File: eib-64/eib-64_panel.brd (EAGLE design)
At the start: 102 x 113 mm, 403 parts, among them J1 DF40-REC, J10 DF40-REC, J11 DF40-REC, J12 DF40-REC, J13 DF40-REC, J14 DF40-REC, J15 DF40-REC, J16 DF40-REC, J2 DF40-REC, J3 DF40-REC, J4 DF40-REC, J5 DF40-REC, J6 DF40-REC, J7 DF40-REC, J8 DF40-REC, J9 DF40-REC

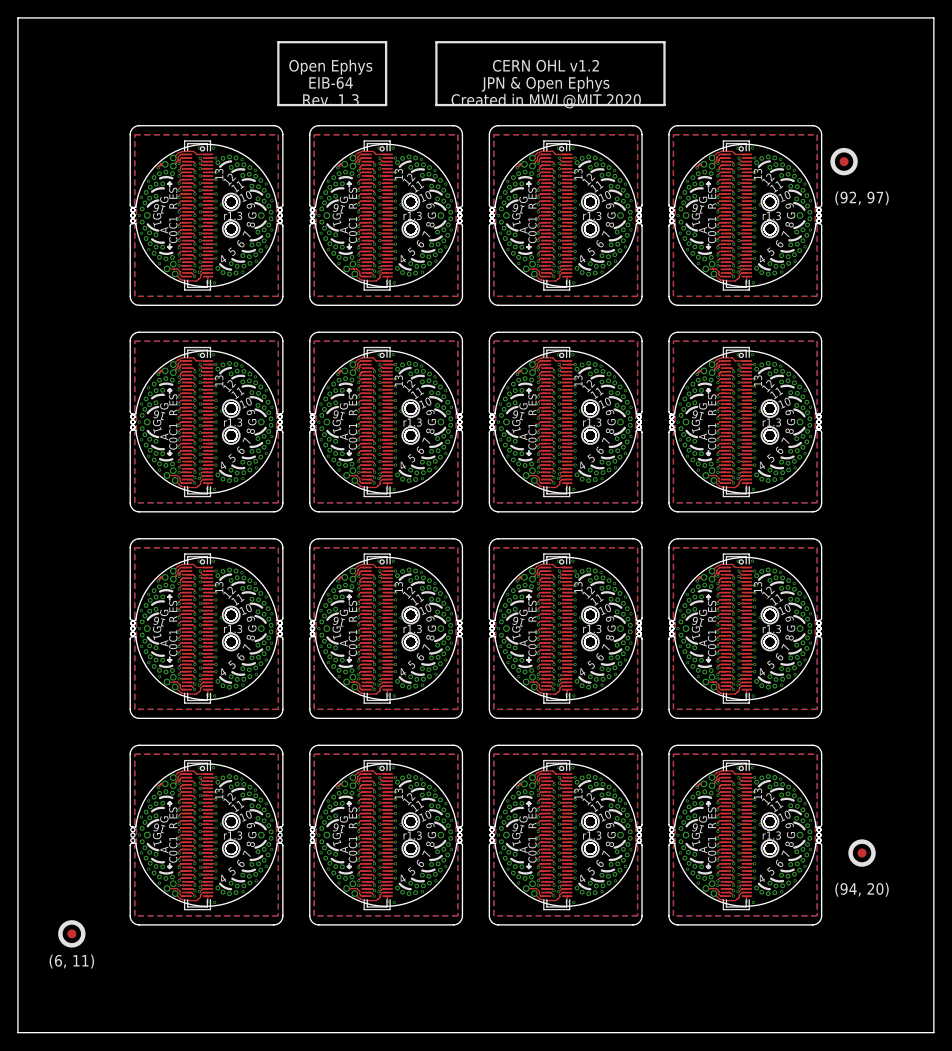
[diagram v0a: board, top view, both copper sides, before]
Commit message: Updated the panel with the new layout.
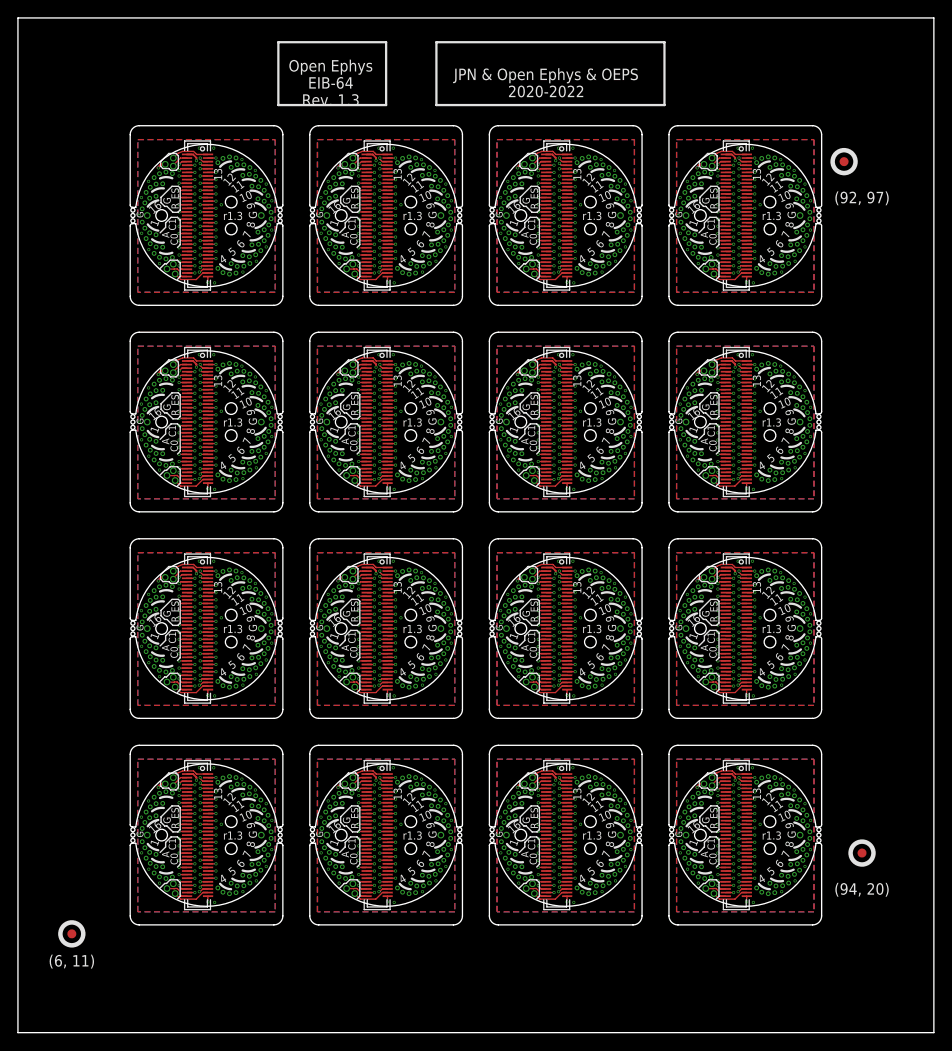
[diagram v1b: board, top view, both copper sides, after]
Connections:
- net GND: now also J1.70; no longer J1.37
- net GND1: now also J2.70; no longer J2.37
- net GND10: now also J11.70; no longer J11.37
- net GND11: now also J12.70; no longer J12.37
- net GND12: now also J13.70; no longer J13.37
- net GND13: now also J14.70; no longer J14.37
- net GND14: now also J15.70; no longer J15.37
- net GND15: now also J16.70; no longer J16.37
- net GND2: now also J3.70; no longer J3.37
- net GND3: now also J4.70; no longer J4.37
- net GND4: now also J5.70; no longer J5.37
- net GND5: now also J6.70; no longer J6.37
- net GND6: now also J7.70; no longer J7.37
- net GND7: now also J8.70; no longer J8.37
- net GND8: now also J9.70; no longer J9.37
- net GND9: now also J10.70; no longer J10.37
- net N$1: now also J1.68; no longer J1.69
- net N$10: now also J1.59; no longer J1.60
- net N$100: now also J2.37; no longer J2.38
- net N$1000: now also J16.55; no longer J16.56
- net N$1001: now also J16.54; no longer J16.55
- net N$1002: now also J16.53; no longer J16.54
- net N$1003: now also J16.52; no longer J16.53
- net N$1004: now also J16.51; no longer J16.52
- net N$1005: now also J16.50; no longer J16.51
- net N$1006: now also J16.49; no longer J16.50
- net N$1007: now also J16.48; no longer J16.49
- net N$1008: now also J16.47; no longer J16.48
- net N$1009: now also J16.46; no longer J16.47
- net N$1010: now also J16.45; no longer J16.46
- net N$1011: now also J16.44; no longer J16.45
- net N$1012: now also J16.43; no longer J16.44
- net N$1013: now also J16.42; no longer J16.43
- net N$1014: now also J16.41; no longer J16.42
- net N$1015: now also J16.40; no longer J16.41
- net N$1016: now also J16.38; no longer J16.39
- net N$1021: now also J16.65; no longer J16.66
- net N$1022: now also J16.67; no longer J16.68
- net N$1023: now also J16.39; no longer J16.40
- net N$1024: now also J16.37; no longer J16.38
- net N$11: now also J1.58; no longer J1.59
- net N$12: now also J1.57; no longer J1.58
- net N$129: now also J3.68; no longer J3.69
- net N$13: now also J1.56; no longer J1.57
- net N$130: now also J3.66; no longer J3.67
- net N$131: now also J3.64; no longer J3.65
- net N$132: now also J3.63; no longer J3.64
- net N$133: now also J3.62; no longer J3.63
- net N$134: now also J3.61; no longer J3.62
- net N$135: now also J3.60; no longer J3.61
- net N$136: now also J3.59; no longer J3.60
- net N$137: now also J3.58; no longer J3.59
- net N$138: now also J3.57; no longer J3.58
- net N$139: now also J3.56; no longer J3.57
- net N$14: now also J1.55; no longer J1.56
- net N$140: now also J3.55; no longer J3.56
- net N$141: now also J3.54; no longer J3.55
- net N$142: now also J3.53; no longer J3.54
- net N$143: now also J3.52; no longer J3.53
- net N$144: now also J3.51; no longer J3.52
- net N$145: now also J3.50; no longer J3.51
- net N$146: now also J3.49; no longer J3.50
- net N$147: now also J3.48; no longer J3.49
- net N$148: now also J3.47; no longer J3.48
- net N$149: now also J3.46; no longer J3.47
- net N$15: now also J1.54; no longer J1.55
- net N$150: now also J3.45; no longer J3.46
- net N$151: now also J3.44; no longer J3.45
- net N$152: now also J3.43; no longer J3.44
- net N$153: now also J3.42; no longer J3.43
- net N$154: now also J3.41; no longer J3.42
- net N$155: now also J3.40; no longer J3.41
- net N$156: now also J3.38; no longer J3.39
- net N$16: now also J1.53; no longer J1.54
- net N$161: now also J3.65; no longer J3.66
- net N$162: now also J3.67; no longer J3.68
- net N$163: now also J3.39; no longer J3.40
- net N$164: now also J3.37; no longer J3.38
- net N$17: now also J1.52; no longer J1.53
- net N$18: now also J1.51; no longer J1.52
- net N$19: now also J1.50; no longer J1.51
- net N$193: now also J4.68; no longer J4.69
- net N$194: now also J4.66; no longer J4.67
- net N$195: now also J4.64; no longer J4.65
- net N$196: now also J4.63; no longer J4.64
- net N$197: now also J4.62; no longer J4.63
- net N$198: now also J4.61; no longer J4.62
- net N$2: now also J1.65; no longer J1.66
- net N$20: now also J1.49; no longer J1.50
- net N$21: now also J1.48; no longer J1.49
- net N$22: now also J1.47; no longer J1.48
- net N$227: now also J4.60; no longer J4.61
- net N$228: now also J4.59; no longer J4.60
- net N$229: now also J4.58; no longer J4.59
- net N$23: now also J1.46; no longer J1.47
- net N$230: now also J4.57; no longer J4.58
- net N$231: now also J4.56; no longer J4.57
- net N$232: now also J4.55; no longer J4.56
- net N$233: now also J4.54; no longer J4.55
- net N$234: now also J4.53; no longer J4.54
- net N$235: now also J4.52; no longer J4.53
- net N$236: now also J4.51; no longer J4.52
- net N$237: now also J4.50; no longer J4.51
- net N$238: now also J4.49; no longer J4.50
- net N$239: now also J4.48; no longer J4.49
- net N$24: now also J1.45; no longer J1.46
- net N$240: now also J4.47; no longer J4.48
- net N$241: now also J4.46; no longer J4.47
- net N$242: now also J4.45; no longer J4.46
- net N$243: now also J4.44; no longer J4.45
- net N$244: now also J4.43; no longer J4.44
- net N$245: now also J4.42; no longer J4.43
- net N$246: now also J4.41; no longer J4.42
- net N$247: now also J4.40; no longer J4.41
- net N$248: now also J4.38; no longer J4.39
- net N$25: now also J1.44; no longer J1.45
- net N$253: now also J4.65; no longer J4.66
- net N$254: now also J4.67; no longer J4.68
- net N$255: now also J4.39; no longer J4.40
- net N$256: now also J4.37; no longer J4.38
- net N$26: now also J1.43; no longer J1.44
- net N$27: now also J1.42; no longer J1.43
- net N$28: now also J1.41; no longer J1.42
- net N$285: now also J5.68; no longer J5.69
- net N$286: now also J5.66; no longer J5.67
- net N$287: now also J5.64; no longer J5.65
- net N$288: now also J5.63; no longer J5.64
- net N$289: now also J5.62; no longer J5.63
- net N$29: now also J1.40; no longer J1.41
- net N$290: now also J5.61; no longer J5.62
- net N$291: now also J5.60; no longer J5.61
- net N$292: now also J5.59; no longer J5.60
- net N$293: now also J5.58; no longer J5.59
- net N$294: now also J5.57; no longer J5.58
- net N$295: now also J5.56; no longer J5.57
- net N$296: now also J5.55; no longer J5.56
- net N$297: now also J5.54; no longer J5.55
- net N$298: now also J5.53; no longer J5.54
- net N$299: now also J5.52; no longer J5.53
- net N$3: now also J1.66; no longer J1.67
- net N$30: now also J1.39; no longer J1.40
- net N$300: now also J5.51; no longer J5.52
- net N$301: now also J5.50; no longer J5.51
- net N$302: now also J5.49; no longer J5.50
- net N$303: now also J5.48; no longer J5.49
- net N$304: now also J5.47; no longer J5.48
- net N$305: now also J5.46; no longer J5.47
- net N$306: now also J5.45; no longer J5.46
- net N$307: now also J5.44; no longer J5.45
- net N$308: now also J5.43; no longer J5.44
- net N$309: now also J5.42; no longer J5.43
- net N$31: now also J1.38; no longer J1.39
- net N$310: now also J5.41; no longer J5.42
- net N$311: now also J5.40; no longer J5.41
- net N$312: now also J5.38; no longer J5.39
- net N$317: now also J5.65; no longer J5.66
- net N$318: now also J5.67; no longer J5.68
- net N$319: now also J5.39; no longer J5.40
- net N$32: now also J1.37; no longer J1.38
- net N$320: now also J5.37; no longer J5.38
- net N$349: now also J6.68; no longer J6.69
- net N$350: now also J6.66; no longer J6.67
- net N$351: now also J6.64; no longer J6.65
- net N$352: now also J6.63; no longer J6.64
- net N$353: now also J6.62; no longer J6.63
- net N$354: now also J6.61; no longer J6.62
- net N$355: now also J6.60; no longer J6.61
- net N$356: now also J6.59; no longer J6.60
- net N$357: now also J6.58; no longer J6.59
- net N$358: now also J6.57; no longer J6.58
- net N$359: now also J6.56; no longer J6.57
- net N$360: now also J6.55; no longer J6.56
- net N$361: now also J6.54; no longer J6.55
- net N$362: now also J6.53; no longer J6.54
- net N$363: now also J6.52; no longer J6.53
- net N$364: now also J6.51; no longer J6.52
- net N$365: now also J6.50; no longer J6.51
- net N$366: now also J6.49; no longer J6.50
- net N$367: now also J6.48; no longer J6.49
- net N$368: now also J6.47; no longer J6.48
- net N$369: now also J6.46; no longer J6.47
- net N$370: now also J6.45; no longer J6.46
- net N$371: now also J6.44; no longer J6.45
- net N$372: now also J6.43; no longer J6.44
- net N$373: now also J6.42; no longer J6.43
- net N$374: now also J6.41; no longer J6.42
- net N$375: now also J6.40; no longer J6.41
- net N$376: now also J6.38; no longer J6.39
- net N$381: now also J6.65; no longer J6.66
- net N$382: now also J6.67; no longer J6.68
- net N$383: now also J6.39; no longer J6.40
- net N$384: now also J6.37; no longer J6.38
- net N$4: now also J1.67; no longer J1.68
- net N$413: now also J7.68; no longer J7.69
- net N$414: now also J7.66; no longer J7.67
- net N$415: now also J7.64; no longer J7.65
- net N$416: now also J7.63; no longer J7.64
- net N$417: now also J7.62; no longer J7.63
- net N$418: now also J7.61; no longer J7.62
- net N$419: now also J7.60; no longer J7.61
- net N$420: now also J7.59; no longer J7.60
- net N$421: now also J7.58; no longer J7.59
- net N$422: now also J7.57; no longer J7.58
- net N$423: now also J7.56; no longer J7.57
- net N$424: now also J7.55; no longer J7.56
- net N$425: now also J7.54; no longer J7.55
- net N$426: now also J7.53; no longer J7.54
- net N$427: now also J7.52; no longer J7.53
- net N$428: now also J7.51; no longer J7.52
- net N$429: now also J7.50; no longer J7.51
- net N$430: now also J7.49; no longer J7.50
- net N$431: now also J7.48; no longer J7.49
- net N$432: now also J7.47; no longer J7.48
- net N$433: now also J7.46; no longer J7.47
- net N$434: now also J7.45; no longer J7.46
- net N$435: now also J7.44; no longer J7.45
- net N$436: now also J7.43; no longer J7.44
- net N$437: now also J7.42; no longer J7.43
- net N$438: now also J7.41; no longer J7.42
- net N$439: now also J7.40; no longer J7.41
- net N$440: now also J7.38; no longer J7.39
- net N$445: now also J7.65; no longer J7.66
- net N$446: now also J7.67; no longer J7.68
- net N$447: now also J7.39; no longer J7.40
- net N$448: now also J7.37; no longer J7.38
- net N$477: now also J8.68; no longer J8.69
- net N$478: now also J8.66; no longer J8.67
- net N$479: now also J8.64; no longer J8.65
- net N$480: now also J8.63; no longer J8.64
- net N$481: now also J8.62; no longer J8.63
- net N$482: now also J8.61; no longer J8.62
- net N$483: now also J8.60; no longer J8.61
- net N$484: now also J8.59; no longer J8.60
- net N$485: now also J8.58; no longer J8.59
- net N$486: now also J8.57; no longer J8.58
- net N$487: now also J8.56; no longer J8.57
- net N$488: now also J8.55; no longer J8.56
- net N$489: now also J8.54; no longer J8.55
- net N$490: now also J8.53; no longer J8.54
- net N$491: now also J8.52; no longer J8.53
- net N$492: now also J8.51; no longer J8.52
- net N$493: now also J8.50; no longer J8.51
- net N$494: now also J8.49; no longer J8.50
- net N$495: now also J8.48; no longer J8.49
- net N$496: now also J8.47; no longer J8.48
- net N$497: now also J8.46; no longer J8.47
- net N$498: now also J8.45; no longer J8.46
- net N$499: now also J8.44; no longer J8.45
- net N$5: now also J1.64; no longer J1.65
- net N$500: now also J8.43; no longer J8.44
- net N$501: now also J8.42; no longer J8.43
- net N$502: now also J8.41; no longer J8.42
- net N$503: now also J8.40; no longer J8.41
- net N$504: now also J8.38; no longer J8.39
- net N$509: now also J8.65; no longer J8.66
- net N$510: now also J8.67; no longer J8.68
- net N$511: now also J8.39; no longer J8.40
- net N$512: now also J8.37; no longer J8.38
- net N$541: now also J9.68; no longer J9.69
- net N$542: now also J9.66; no longer J9.67
- net N$543: now also J9.64; no longer J9.65
- net N$544: now also J9.63; no longer J9.64
- net N$545: now also J9.62; no longer J9.63
- net N$546: now also J9.61; no longer J9.62
- net N$547: now also J9.60; no longer J9.61
- net N$548: now also J9.59; no longer J9.60
- net N$549: now also J9.58; no longer J9.59
- net N$550: now also J9.57; no longer J9.58
- net N$551: now also J9.56; no longer J9.57
- net N$552: now also J9.55; no longer J9.56
- net N$553: now also J9.54; no longer J9.55
- net N$554: now also J9.53; no longer J9.54
- net N$555: now also J9.52; no longer J9.53
- net N$556: now also J9.51; no longer J9.52
- net N$557: now also J9.50; no longer J9.51
- net N$558: now also J9.49; no longer J9.50
- net N$559: now also J9.48; no longer J9.49
- net N$560: now also J9.47; no longer J9.48
- net N$561: now also J9.46; no longer J9.47
- net N$562: now also J9.45; no longer J9.46
- net N$563: now also J9.44; no longer J9.45
- net N$564: now also J9.43; no longer J9.44
- net N$565: now also J9.42; no longer J9.43
- net N$566: now also J9.41; no longer J9.42
- net N$567: now also J9.40; no longer J9.41
- net N$568: now also J9.38; no longer J9.39
- net N$573: now also J9.65; no longer J9.66
- net N$574: now also J9.67; no longer J9.68
- net N$575: now also J9.39; no longer J9.40
- net N$576: now also J9.37; no longer J9.38
- net N$6: now also J1.63; no longer J1.64
- net N$605: now also J10.68; no longer J10.69
- net N$606: now also J10.66; no longer J10.67
- net N$607: now also J10.64; no longer J10.65
- net N$608: now also J10.63; no longer J10.64
- net N$609: now also J10.62; no longer J10.63
- net N$610: now also J10.61; no longer J10.62
- net N$611: now also J10.60; no longer J10.61
- net N$612: now also J10.59; no longer J10.60
- net N$613: now also J10.58; no longer J10.59
- net N$614: now also J10.57; no longer J10.58
- net N$615: now also J10.56; no longer J10.57
- net N$616: now also J10.55; no longer J10.56
- net N$617: now also J10.54; no longer J10.55
- net N$618: now also J10.53; no longer J10.54
- net N$619: now also J10.52; no longer J10.53
- net N$620: now also J10.51; no longer J10.52
- net N$621: now also J10.50; no longer J10.51
- net N$622: now also J10.49; no longer J10.50
- net N$623: now also J10.48; no longer J10.49
- net N$624: now also J10.47; no longer J10.48
- net N$625: now also J10.46; no longer J10.47
- net N$626: now also J10.45; no longer J10.46
- net N$627: now also J10.44; no longer J10.45
- net N$628: now also J10.43; no longer J10.44
- net N$629: now also J10.42; no longer J10.43
- net N$630: now also J10.41; no longer J10.42
- net N$631: now also J10.40; no longer J10.41
- net N$632: now also J10.38; no longer J10.39
- net N$637: now also J10.65; no longer J10.66
- net N$638: now also J10.67; no longer J10.68
- net N$639: now also J10.39; no longer J10.40
- net N$640: now also J10.37; no longer J10.38
- net N$65: now also J2.68; no longer J2.69
- net N$66: now also J2.66; no longer J2.67
- net N$669: now also J11.68; no longer J11.69
- net N$67: now also J2.64; no longer J2.65
- net N$670: now also J11.66; no longer J11.67
- net N$671: now also J11.64; no longer J11.65
- net N$672: now also J11.63; no longer J11.64
- net N$673: now also J11.62; no longer J11.63
- net N$674: now also J11.61; no longer J11.62
- net N$675: now also J11.60; no longer J11.61
- net N$676: now also J11.59; no longer J11.60
- net N$677: now also J11.58; no longer J11.59
- net N$678: now also J11.57; no longer J11.58
- net N$679: now also J11.56; no longer J11.57
- net N$68: now also J2.63; no longer J2.64
- net N$680: now also J11.55; no longer J11.56
- net N$681: now also J11.54; no longer J11.55
- net N$682: now also J11.53; no longer J11.54
- net N$683: now also J11.52; no longer J11.53
- net N$684: now also J11.51; no longer J11.52
- net N$685: now also J11.50; no longer J11.51
- net N$686: now also J11.49; no longer J11.50
- net N$687: now also J11.48; no longer J11.49
- net N$688: now also J11.47; no longer J11.48
- net N$689: now also J11.46; no longer J11.47
- net N$69: now also J2.62; no longer J2.63
- net N$690: now also J11.45; no longer J11.46
- net N$691: now also J11.44; no longer J11.45
- net N$692: now also J11.43; no longer J11.44
- net N$693: now also J11.42; no longer J11.43
- net N$694: now also J11.41; no longer J11.42
- net N$695: now also J11.40; no longer J11.41
- net N$696: now also J11.38; no longer J11.39
- net N$7: now also J1.62; no longer J1.63
- net N$70: now also J2.61; no longer J2.62
- net N$701: now also J11.65; no longer J11.66
- net N$702: now also J11.67; no longer J11.68
- net N$703: now also J11.39; no longer J11.40
- net N$704: now also J11.37; no longer J11.38
- net N$71: now also J2.60; no longer J2.61
- net N$72: now also J2.59; no longer J2.60
- net N$73: now also J2.58; no longer J2.59
- net N$733: now also J12.68; no longer J12.69
- net N$734: now also J12.66; no longer J12.67
- net N$735: now also J12.64; no longer J12.65
- net N$736: now also J12.63; no longer J12.64
- net N$737: now also J12.62; no longer J12.63
- net N$738: now also J12.61; no longer J12.62
- net N$739: now also J12.60; no longer J12.61
- net N$74: now also J2.57; no longer J2.58
- net N$740: now also J12.59; no longer J12.60
- net N$741: now also J12.58; no longer J12.59
- net N$742: now also J12.57; no longer J12.58
- net N$743: now also J12.56; no longer J12.57
- net N$744: now also J12.55; no longer J12.56
- net N$745: now also J12.54; no longer J12.55
- net N$746: now also J12.53; no longer J12.54
- net N$747: now also J12.52; no longer J12.53
- net N$748: now also J12.51; no longer J12.52
- net N$749: now also J12.50; no longer J12.51
- net N$75: now also J2.56; no longer J2.57
- net N$750: now also J12.49; no longer J12.50
- net N$751: now also J12.48; no longer J12.49
- net N$752: now also J12.47; no longer J12.48
- net N$753: now also J12.46; no longer J12.47
- net N$754: now also J12.45; no longer J12.46
- net N$755: now also J12.44; no longer J12.45
- net N$756: now also J12.43; no longer J12.44
- net N$757: now also J12.42; no longer J12.43
- net N$758: now also J12.41; no longer J12.42
- net N$759: now also J12.40; no longer J12.41
- net N$76: now also J2.55; no longer J2.56
- net N$760: now also J12.38; no longer J12.39
- net N$765: now also J12.65; no longer J12.66
- net N$766: now also J12.67; no longer J12.68
- net N$767: now also J12.39; no longer J12.40
- net N$768: now also J12.37; no longer J12.38
- net N$77: now also J2.54; no longer J2.55
- net N$78: now also J2.53; no longer J2.54
- net N$79: now also J2.52; no longer J2.53
- net N$797: now also J13.68; no longer J13.69
- net N$798: now also J13.66; no longer J13.67
- net N$799: now also J13.64; no longer J13.65
- net N$8: now also J1.61; no longer J1.62
- net N$80: now also J2.51; no longer J2.52
- net N$800: now also J13.63; no longer J13.64
- net N$801: now also J13.62; no longer J13.63
- net N$802: now also J13.61; no longer J13.62
- net N$803: now also J13.60; no longer J13.61
- net N$804: now also J13.59; no longer J13.60
- net N$805: now also J13.58; no longer J13.59
- net N$806: now also J13.57; no longer J13.58
- net N$807: now also J13.56; no longer J13.57
- net N$808: now also J13.55; no longer J13.56
- net N$809: now also J13.54; no longer J13.55
- net N$81: now also J2.50; no longer J2.51
- net N$810: now also J13.53; no longer J13.54
- net N$811: now also J13.52; no longer J13.53
- net N$812: now also J13.51; no longer J13.52
- net N$813: now also J13.50; no longer J13.51
- net N$814: now also J13.49; no longer J13.50
- net N$815: now also J13.48; no longer J13.49
- net N$816: now also J13.47; no longer J13.48
- net N$817: now also J13.46; no longer J13.47
- net N$818: now also J13.45; no longer J13.46
- net N$819: now also J13.44; no longer J13.45
- net N$82: now also J2.49; no longer J2.50
- net N$820: now also J13.43; no longer J13.44
- net N$821: now also J13.42; no longer J13.43
- net N$822: now also J13.41; no longer J13.42
- net N$823: now also J13.40; no longer J13.41
- net N$824: now also J13.38; no longer J13.39
- net N$829: now also J13.65; no longer J13.66
- net N$83: now also J2.48; no longer J2.49
- net N$830: now also J13.67; no longer J13.68
- net N$831: now also J13.39; no longer J13.40
- net N$832: now also J13.37; no longer J13.38
- net N$84: now also J2.47; no longer J2.48
- net N$85: now also J2.46; no longer J2.47
- net N$86: now also J2.45; no longer J2.46
- net N$861: now also J14.68; no longer J14.69
- net N$862: now also J14.66; no longer J14.67
- net N$863: now also J14.64; no longer J14.65
- net N$864: now also J14.63; no longer J14.64
- net N$865: now also J14.62; no longer J14.63
- net N$866: now also J14.61; no longer J14.62
- net N$867: now also J14.60; no longer J14.61
- net N$868: now also J14.59; no longer J14.60
- net N$869: now also J14.58; no longer J14.59
- net N$87: now also J2.44; no longer J2.45
- net N$870: now also J14.57; no longer J14.58
- net N$871: now also J14.56; no longer J14.57
- net N$872: now also J14.55; no longer J14.56
- net N$873: now also J14.54; no longer J14.55
- net N$874: now also J14.53; no longer J14.54
- net N$875: now also J14.52; no longer J14.53
- net N$876: now also J14.51; no longer J14.52
- net N$877: now also J14.50; no longer J14.51
- net N$878: now also J14.49; no longer J14.50
- net N$879: now also J14.48; no longer J14.49
- net N$88: now also J2.43; no longer J2.44
- net N$880: now also J14.47; no longer J14.48
- net N$881: now also J14.46; no longer J14.47
- net N$882: now also J14.45; no longer J14.46
- net N$883: now also J14.44; no longer J14.45
- net N$884: now also J14.43; no longer J14.44
- net N$885: now also J14.42; no longer J14.43
- net N$886: now also J14.41; no longer J14.42
- net N$887: now also J14.40; no longer J14.41
- net N$888: now also J14.38; no longer J14.39
- net N$89: now also J2.42; no longer J2.43
- net N$893: now also J14.65; no longer J14.66
- net N$894: now also J14.67; no longer J14.68
- net N$895: now also J14.39; no longer J14.40
- net N$896: now also J14.37; no longer J14.38
- net N$9: now also J1.60; no longer J1.61
- net N$90: now also J2.41; no longer J2.42
- net N$91: now also J2.40; no longer J2.41
- net N$92: now also J2.38; no longer J2.39
- net N$925: now also J15.68; no longer J15.69
- net N$926: now also J15.66; no longer J15.67
- net N$927: now also J15.64; no longer J15.65
- net N$928: now also J15.63; no longer J15.64
- net N$929: now also J15.62; no longer J15.63
- net N$930: now also J15.61; no longer J15.62
- net N$931: now also J15.60; no longer J15.61
- net N$932: now also J15.59; no longer J15.60
- net N$933: now also J15.58; no longer J15.59
- net N$934: now also J15.57; no longer J15.58
- net N$935: now also J15.56; no longer J15.57
- net N$936: now also J15.55; no longer J15.56
- net N$937: now also J15.54; no longer J15.55
- net N$938: now also J15.53; no longer J15.54
- net N$939: now also J15.52; no longer J15.53
- net N$940: now also J15.51; no longer J15.52
- net N$941: now also J15.50; no longer J15.51
- net N$942: now also J15.49; no longer J15.50
- net N$943: now also J15.48; no longer J15.49
- net N$944: now also J15.47; no longer J15.48
- net N$945: now also J15.46; no longer J15.47
- net N$946: now also J15.45; no longer J15.46
- net N$947: now also J15.44; no longer J15.45
- net N$948: now also J15.43; no longer J15.44
- net N$949: now also J15.42; no longer J15.43
- net N$950: now also J15.41; no longer J15.42
- net N$951: now also J15.40; no longer J15.41
- net N$952: now also J15.38; no longer J15.39
- net N$957: now also J15.65; no longer J15.66
- net N$958: now also J15.67; no longer J15.68
- net N$959: now also J15.39; no longer J15.40
- net N$960: now also J15.37; no longer J15.38
- net N$97: now also J2.65; no longer J2.66
- net N$98: now also J2.67; no longer J2.68
- net N$989: now also J16.68; no longer J16.69
- net N$99: now also J2.39; no longer J2.40
- net N$990: now also J16.66; no longer J16.67
- net N$991: now also J16.64; no longer J16.65
- net N$992: now also J16.63; no longer J16.64
- net N$993: now also J16.62; no longer J16.63
- net N$994: now also J16.61; no longer J16.62
- net N$995: now also J16.60; no longer J16.61
- net N$996: now also J16.59; no longer J16.60
- net N$997: now also J16.58; no longer J16.59
- net N$998: now also J16.57; no longer J16.58
- net N$999: now also J16.56; no longer J16.57
- net REF: now also J1.69; no longer J1.70
- net REF1: now also J2.69; no longer J2.70
- net REF10: now also J11.69; no longer J11.70
- net REF11: now also J12.69; no longer J12.70
- net REF12: now also J13.69; no longer J13.70
- net REF13: now also J14.69; no longer J14.70
- net REF14: now also J15.69; no longer J15.70
- net REF15: now also J16.69; no longer J16.70
- net REF2: now also J3.69; no longer J3.70
- net REF3: now also J4.69; no longer J4.70
- net REF4: now also J5.69; no longer J5.70
- net REF5: now also J6.69; no longer J6.70
- net REF6: now also J7.69; no longer J7.70
- net REF7: now also J8.69; no longer J8.70
- net REF8: now also J9.69; no longer J9.70
- net REF9: now also J10.69; no longer J10.70
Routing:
- net N$567: track 7.07 -> 6.40 mm
- net N$311: track 7.07 -> 6.40 mm
- net N$695: track 7.07 -> 6.40 mm
- net N$631: track 7.07 -> 6.40 mm
- net N$439: track 7.07 -> 6.40 mm
- net N$375: track 7.07 -> 6.40 mm
- net N$29: track 7.07 -> 6.40 mm
- net N$91: track 7.07 -> 6.40 mm
- net N$823: track 7.07 -> 6.40 mm
- net N$155: track 7.07 -> 6.40 mm
- net N$951: track 7.07 -> 6.40 mm
- net N$887: track 7.07 -> 6.40 mm
- net N$759: track 7.07 -> 6.40 mm
- net N$503: track 7.07 -> 6.40 mm
- net N$247: track 7.07 -> 6.40 mm
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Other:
- board text added: "EIB-64, r1.3 Open Ephys"
- board text added: "JPN & Open Ephys & OEPS 2020-2022"
- board text removed: "CERN OHL v1.2 JPN & Open Ephys Created in MWL@MIT 2020"
- board text removed: "EIB-64, r1.2 JPN & Open Ephys OHL v1.2 '19"
